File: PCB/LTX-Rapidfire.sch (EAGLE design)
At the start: 52 parts, among them J1 F-1X08-SIP-100-40Y, Q1 2N3904, Q10 SS8550D, Q11 2N3906, Q12 2N3906, Q13 2N3904, Q2 2N3906, Q3 2N3904, Q4 2N3904, Q5 2N3904, Q6 2N3906, Q7 2N3906, Q8 2N3906, Q9 2N3904, SW1 F-1X02-SIP-100-40, U2 Z8F082ADIL-8

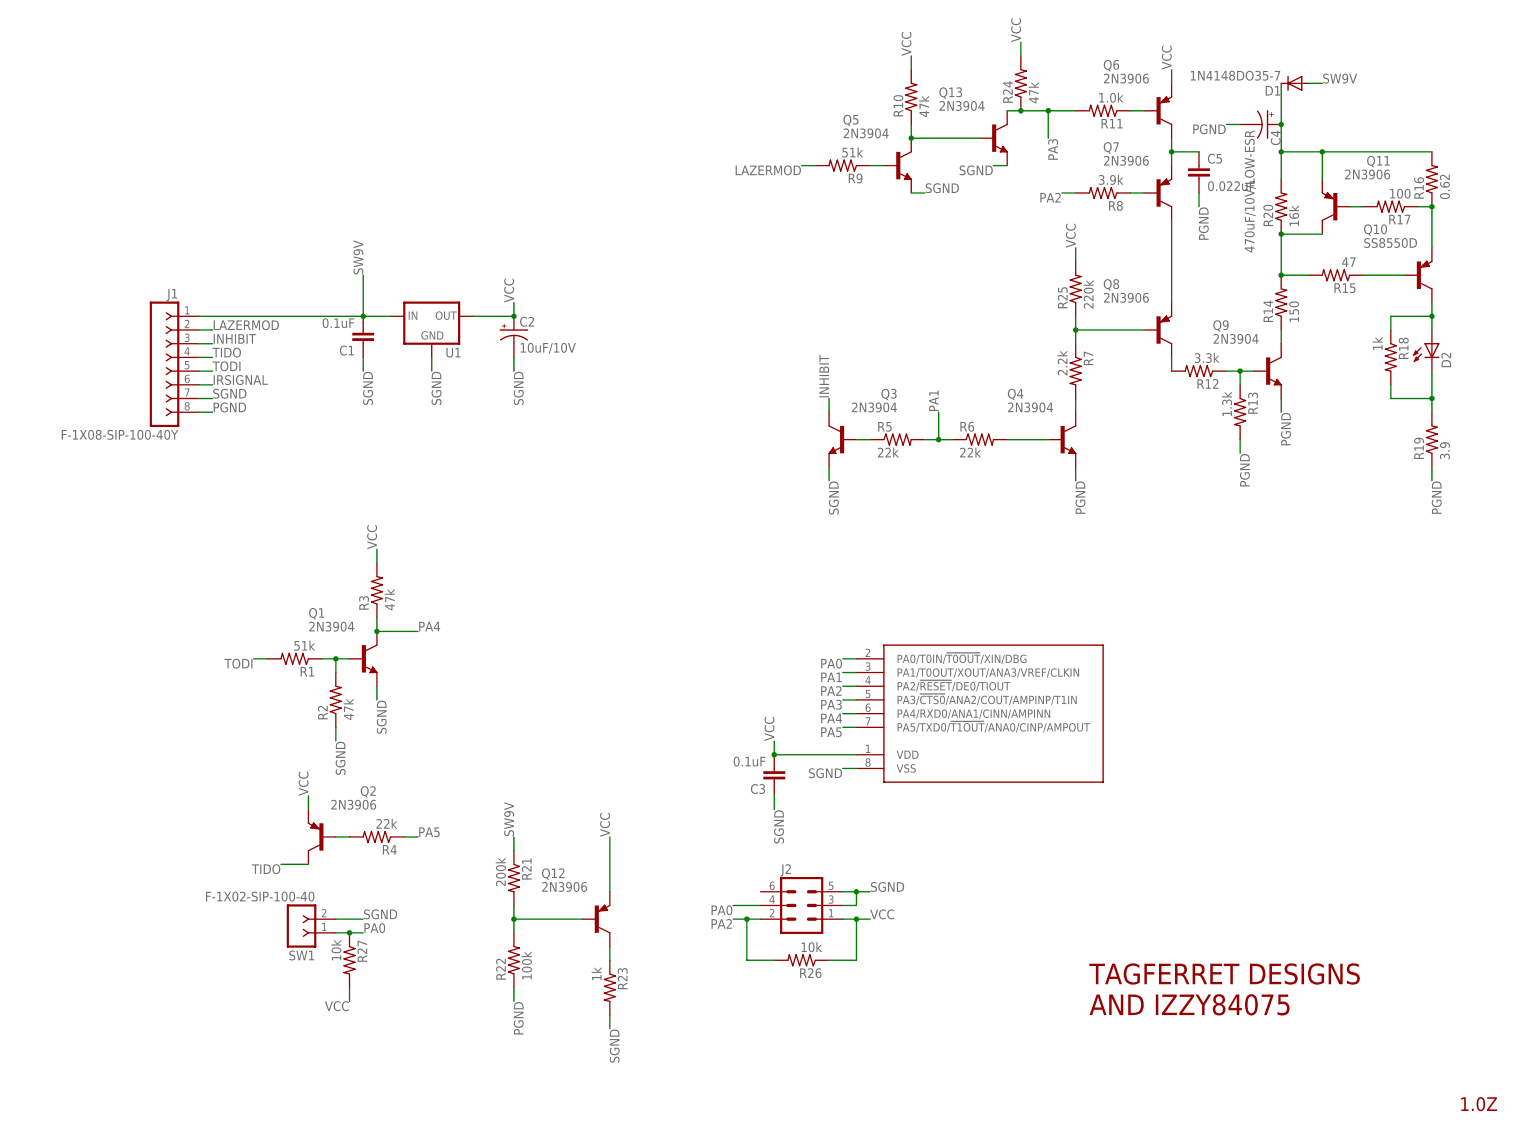
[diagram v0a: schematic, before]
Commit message: Labeled part numbers in schematic. Prep for SMD-ification
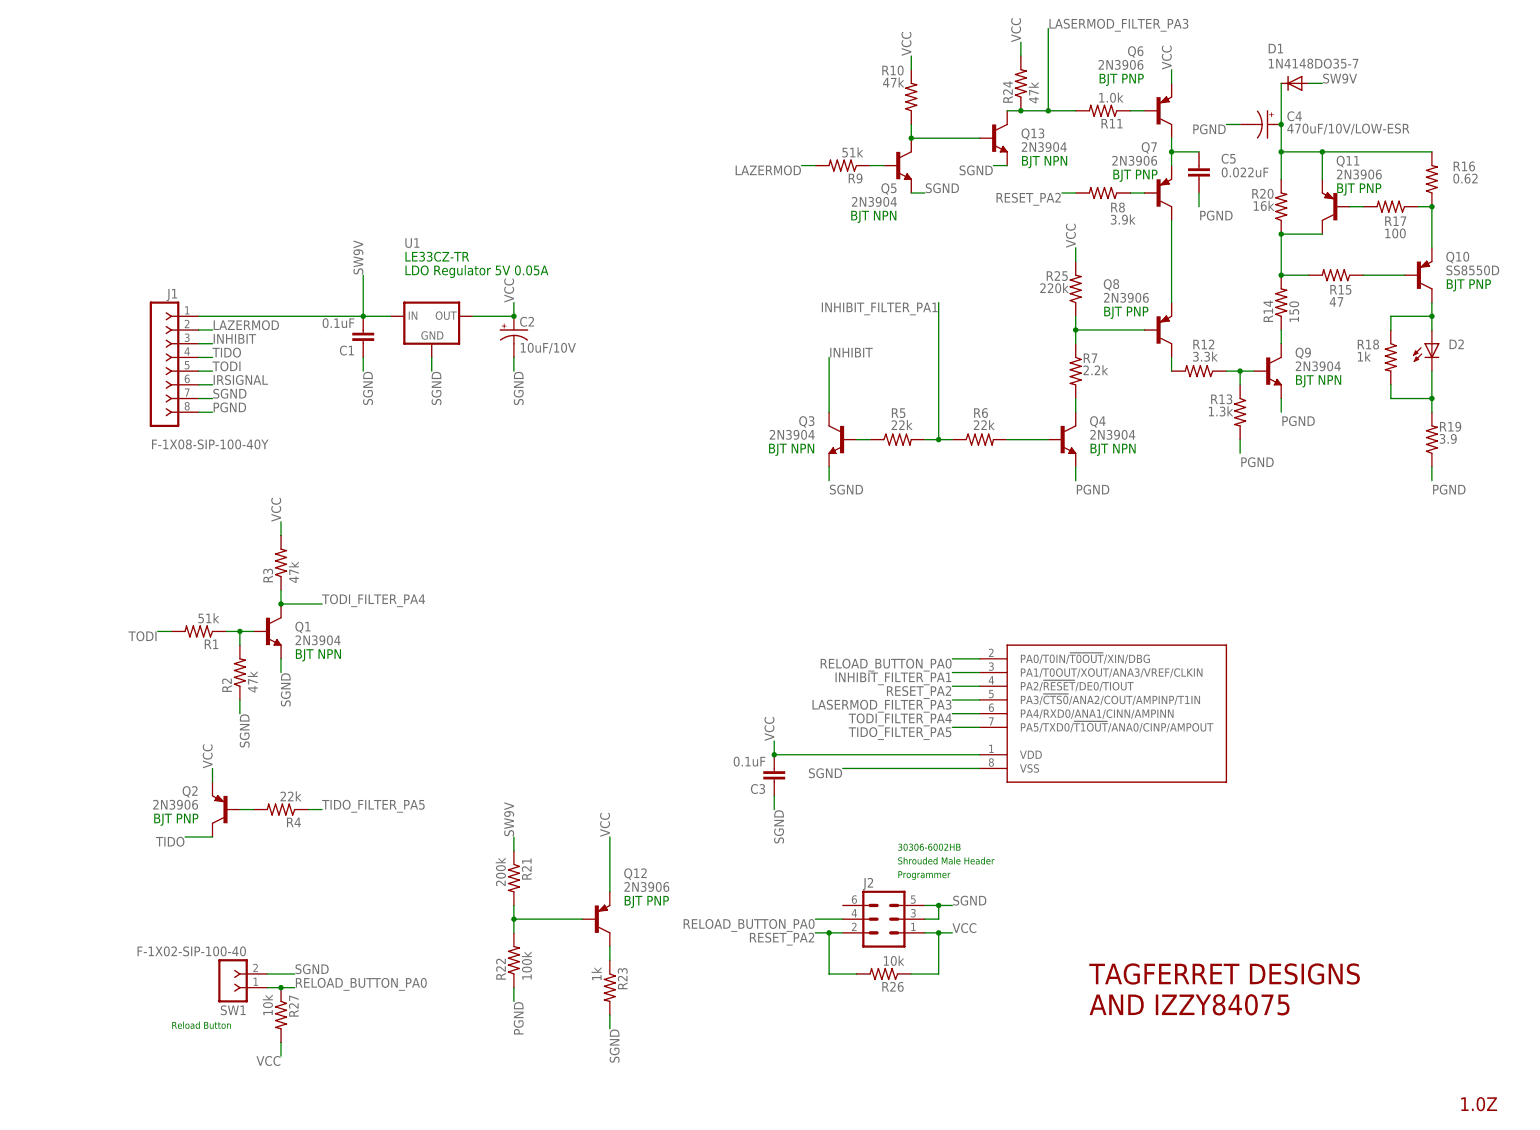
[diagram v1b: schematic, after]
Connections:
- net PA0 renamed RELOAD_BUTTON_PA0
- net PA1 renamed INHIBIT_FILTER_PA1
- net PA2 renamed RESET_PA2
- net PA3 renamed LASERMOD_FILTER_PA3
- net PA4 renamed TODI_FILTER_PA4
- net PA5 renamed TIDO_FILTER_PA5
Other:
- note added: "30306-6002HB"
- note added: "BJT NPN"
- note added: "BJT PNP"
- note added: "LDO Regulator 5V 0.05A"
- note added: "LE33CZ-TR"
- note added: "Programmer"
- note added: "Reload Button"
- note added: "Shrouded Male Header"
- moved on the sheet: J2, Q1, Q2, R1, R2, R26, R27, R3, R4, SW1

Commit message: Swapped basics to SMD
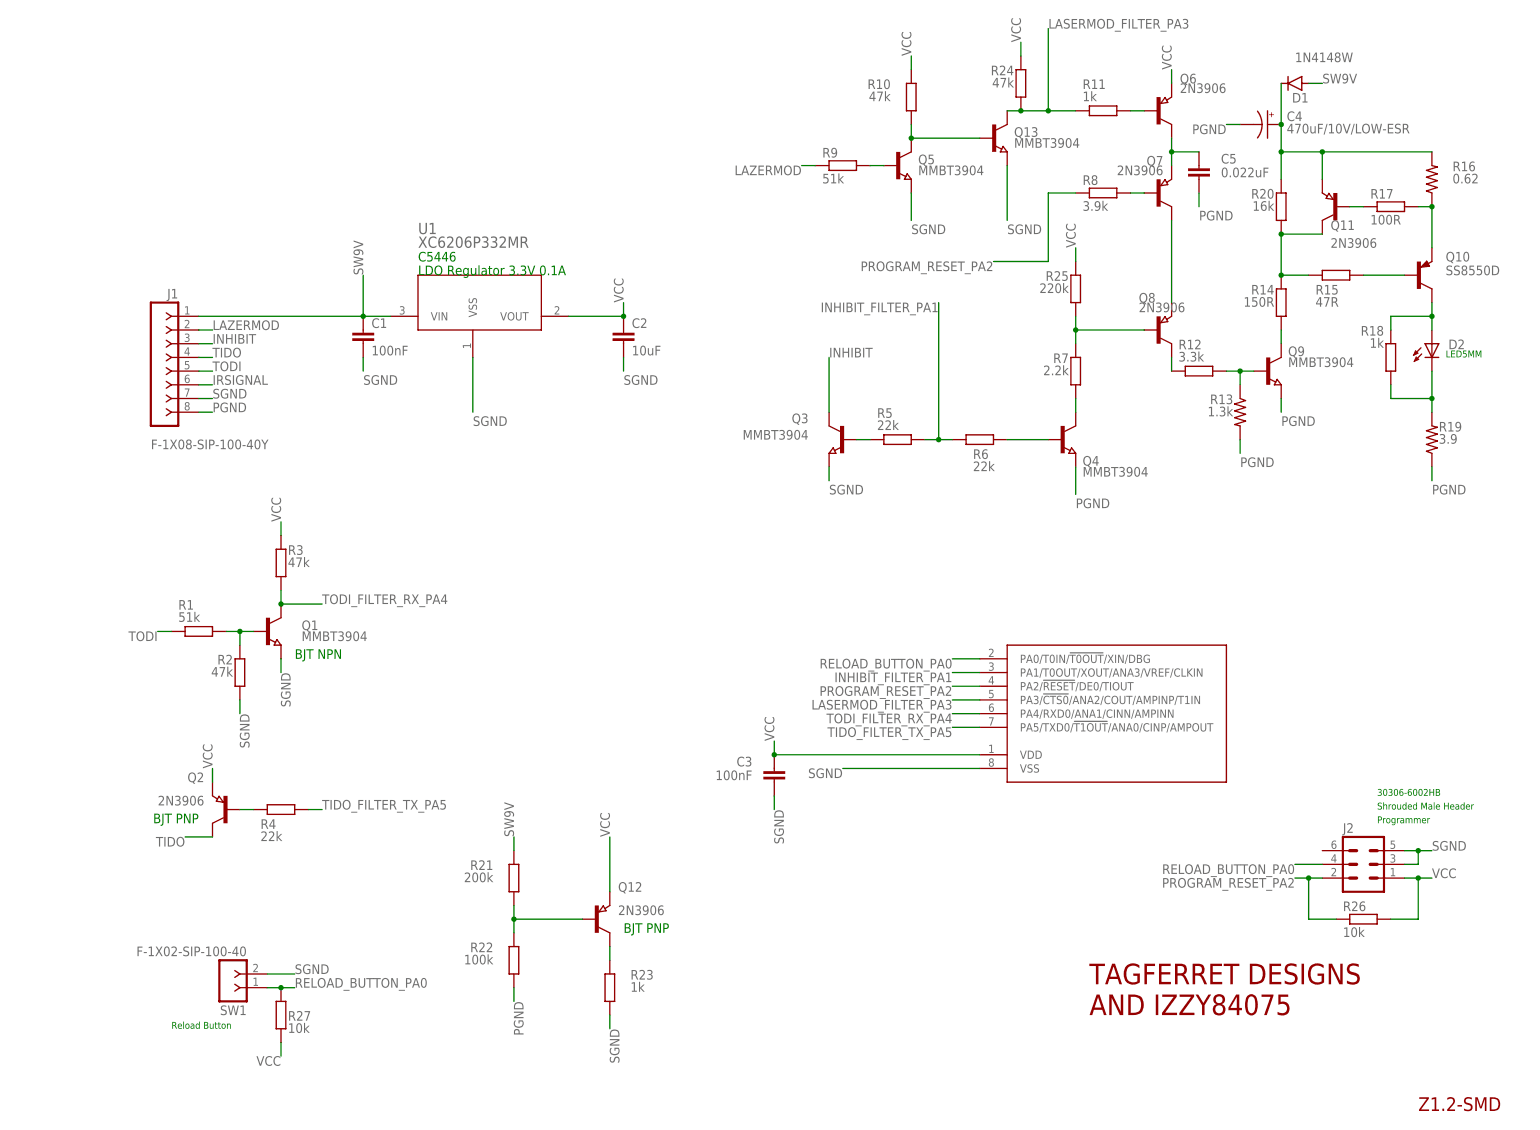
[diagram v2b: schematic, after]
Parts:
- C1, C3: value 0.1uF -> 100nF; device rcl:C-EU025-025X050 -> JLC PCB Basic Parts_loc:C_100NF/50V_0603
- C2: value 10uF/10V -> 10uF; device rcl:CPOL-USE2-4 -> JLC PCB Basic Parts_loc:C_10UF/25V_0603
- D1: value 1N4148DO35-7 -> 1N4148W; device diode:1N4148DO35-7 -> JLC PCB Basic Parts_loc:D_1N4148W_ST_SOD123
- Q1, Q13, Q3, Q4, Q5, Q9: value 2N3904 -> MMBT3904; device transistor:2N3904 -> JLC PCB Basic Parts_loc:T_NPN_MMBT3904_CHANGJ_SOT23-BEC
- Q11, Q12, Q2, Q6, Q7, Q8: device transistor-pnp:2N3906 -> JLC PCB Basic Parts_loc:T_PNP_MMBT5401_CHANGJ_SOT23-BEC; LCSC_DATASHEET (none) -> https://datasheet.lcsc.com/lcsc/1810111520_KEC-Semicon-2N39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; LCSC_PART (none) -> C147294; PROPERTIES (none) -> 40V 350mW 200mA 100@10mA,1V 250MHz 400mV@50mA,5mA PNP
- R1, R9: device rcl:R-US_0204/7 -> JLC PCB Basic Parts_loc:R_51K_0603
- R10, R2, R24, R3: device rcl:R-US_0204/2V -> JLC PCB Basic Parts_loc:R_47K_0603
- R11: value 1.0k -> 1k; device rcl:R-US_0204/7 -> JLC PCB Basic Parts_loc:R_1K_0603
- R12: device rcl:R-US_0204/7 -> JLC PCB Basic Parts_loc:R_3.3K_0603
- R14: value 150 -> 150R; device rcl:R-US_0204/7 -> JLC PCB Basic Parts_loc:R_150R_0603
- R15: value 47 -> 47R; device rcl:R-US_0204/7 -> JLC PCB Basic Parts_loc:R_47R_0603
- R17: value 100 -> 100R; device rcl:R-US_0204/2V -> JLC PCB Basic Parts_loc:R_100R_0603
- R18: device rcl:R-US_0204/2V -> JLC PCB Basic Parts_loc:R_1K_0603
- R20: device rcl:R-US_0204/2V -> JLC PCB Basic Parts_loc:R_16K_0805
- R21: device rcl:R-US_0204/7 -> JLC PCB Basic Parts_loc:R_200K_0603
- R22: device rcl:R-US_0204/2V -> JLC PCB Basic Parts_loc:R_100K_0603
- R23: device rcl:R-US_0204/7 -> JLC PCB Basic Parts_loc:R_1K_0603
- R25: device rcl:R-US_0204/2V -> JLC PCB Basic Parts_loc:R_220K_0603
- R26, R27: device rcl:R-US_0204/2V -> JLC PCB Basic Parts_loc:R_10K_0603
- R4, R5, R6: device rcl:R-US_0204/7 -> JLC PCB Basic Parts_loc:R_22K_0603
- R7: device rcl:R-US_0204/7 -> JLC PCB Basic Parts_loc:R_2.2K_0603
- R8: device rcl:R-US_0204/7 -> JLC PCB Basic Parts_loc:R_3.9K_0603
- U1: value (none) -> XC6206P332MR; device v-reg:78LXX -> LTX-Rapidfire:XC6206P332MR
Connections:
- net TODI_FILTER_PA4 renamed TODI_FILTER_RX_PA4
- removed net RESET_PA2: J2.2, R26.2, R8.2, U2.PA2/!RESET!/DE0/TIOUT
- removed net TIDO_FILTER_PA5: R4.1, U2.PA5/TXD0/!T1OUT!/ANA0/CINP/AMPOUT
- new net PROGRAM_RESET_PA2: J2.2, R26.1, R8.1, U2.PA2/!RESET!/DE0/TIOUT
- new net TIDO_FILTER_TX_PA5: R4.2, U2.PA5/TXD0/!T1OUT!/ANA0/CINP/AMPOUT
- net LASERMOD_FILTER_PA3: now also R11.1; no longer R11.2
- net LAZERMOD: now also R9.1; no longer R9.2
- net N$1: now also R17.1; no longer R17.2
- net N$10: now also R12.1; no longer R12.2
- net N$12: now also R7.2; no longer R7.1
- net N$13: now also R8.2; no longer R8.1
- net N$14: now also R7.1; no longer R7.2
- net N$17: now also R23.2; no longer R23.1
- net N$19: now also R11.2; no longer R11.1
- net N$20: now also R21.1; no longer R21.2
- net N$22: now also R9.2; no longer R9.1
- net N$24: now also R1.2; no longer R1.1
- net N$25: now also R4.1; no longer R4.2
- net N$3: now also R17.2; no longer R17.1
- net N$4: now also R15.1; no longer R15.2
- net N$5: now also R15.2; no longer R15.1
- net N$7: now also R18.1; no longer R18.2
- net N$8: now also R18.2; no longer R18.1
- net N$9: now also R12.2; no longer R12.1
- net RELOAD_BUTTON_PA0: now also R27.2; no longer R27.1
- net SGND: now also C1.2, C2.2, C3.2, R23.1, U1.VSS; no longer C1.1, C2.-, C3.1, R23.2, U1.GND
- net SW9V: now also C1.1, R21.2, U1.VIN; no longer C1.2, R21.1, U1.IN
- net TODI: now also R1.1; no longer R1.2
- net VCC: now also C2.1, C3.1, R26.2, R27.1, U1.VOUT; no longer C2.+, C3.2, R26.1, R27.2, U1.OUT
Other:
- note added: "C5446"
- note added: "LDO Regulator 3.3V 0.1A"
- note added: "LED5MM"
- note added: "Z1.2-SMD"
- note removed: "1.0Z"
- note removed: "LDO Regulator 5V 0.05A"
- note removed: "LE33CZ-TR"
- moved on the sheet: J2

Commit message: Part lists and gerbers for JLC
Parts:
- C4: LCSC (none) -> C43332; LCSC_PART (none) -> C43332
- C5: value 0.022uF -> 22nF; device rcl:C-EU025-025X050 -> JLC PCB Basic Parts_loc:C_22NF/50V_0603
- Q10: LCSC_PART (none) -> C118551
- R13: device rcl:R-US_0204/2V -> JLC PCB Basic Parts_loc:R_2.2K_0603; LCSC_DATASHEET (none) -> https://datasheet.lcsc.com/lcsc/2206010130_UNI-ROYAL-Uniroy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; LCSC_PART (none) -> C22767; PROPERTIES (none) -> 100mW Thick Film Resistors 75V ±100ppm/℃ ±1% -55℃~+155℃ 1.3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
- R16: value 0.62 -> 0.62R 1W; device rcl:R-US_0204/7 -> resistor:R-US_R2512; LCSC_PART (none) -> C705623
- R19: value 3.9 -> 3.9R 1W; device rcl:R-US_0207/10 -> resistor:R-US_R2512; LCSC_PART (none) -> C66801
- U1: LCSC_PART (none) -> C5446
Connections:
- net N$9: now also R13.2; no longer R13.1
- net PGND: now also R13.1; no longer R13.2
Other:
- note added: "1W 1.5A"

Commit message: Swapped chip and routed pcb
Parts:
- removed C3: 100nF, JLC PCB Basic Parts_loc:C_100NF/50V_0603
- removed J2: (no value), izzy:MA03-2
- removed R26: 10k, JLC PCB Basic Parts_loc:R_10K_0603
- removed U2: Z8F082ADIL-8, izzy:Z8F082ADIL-8
- added C6: 100nF, JLC PCB Basic Parts_loc:C_100NF/50V_0603
- added JP1: (no value), adafruit:PINHD-1X3
- added R28: 1K, SparkFun-Resistors:2.2KOHM-0402-1/16W-1%
- added U3: ATTINY1616-MNRVQFN20_3X3_MCH-M, attiny1616:ATTINY1616-MNRVQFN20_3X3_MCH-M
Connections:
- net INHIBIT renamed INHIBIT_OUT
- net LAZERMOD renamed LAZERMOD_IN
- net N$2 renamed PROTECTED_9V
- net SW9V renamed +9V
- removed net INHIBIT_FILTER_PA1: R5.2, R6.1, U2.PA1/T0OUT/XOUT/ANA3/VREF/CLKIN
- removed net LASERMOD_FILTER_PA3: Q13.C, R11.1, R24.1, U2.PA3/!CTS0!/ANA2/COUT/AMPINP/T1IN
- removed net PROGRAM_RESET_PA2: J2.2, R26.1, R8.1, U2.PA2/!RESET!/DE0/TIOUT
- removed net RELOAD_BUTTON_PA0: J2.4, R27.2, SW1.1, U2.PA0/T0IN/!T0OUT!/XIN/DBG
- removed net TIDO_FILTER_TX_PA5: R4.2, U2.PA5/TXD0/!T1OUT!/ANA0/CINP/AMPOUT
- removed net TODI_FILTER_RX_PA4: Q1.C, R3.1, U2.PA4/RXD0/ANA1/CINN/AMPINN
- new net INHIBIT_PB1: R5.2, R6.1, U3.PB1
- new net LASERMOD_IN_PB3: Q13.C, R11.1, R24.1, U3.TOSC/PB3
- new net PROGRAM_RESET_PA0: R28.1, R8.1, U3.PA0/!RESET/UPDI
- new net RELOAD_BUTTON_PB0: R27.2, SW1.2, U3.PB0
- new net TIDO_FILTER_TX_PA1: R4.2, U3.PA1
- new net TODI_FILTER_RX_PA2: Q1.C, R3.1, U3.PA2
- new net UPDI: JP1.3, R28.2
- net SGND: now also C6.2, JP1.2, SW1.1, U3.GND; no longer C3.2, J2.3, J2.5, SW1.2, U2.VSS
- net VCC: now also C6.1, JP1.1, U3.VDD; no longer C3.1, J2.1, R26.2, U2.VDD
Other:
- note added: "0 16 15"
- note added: "10 9 8 7 6"
- note added: "14 13 12 11"
- note added: "5 4 3 2 1"
- note added: "ARDUINO"
- note added: "C507118"
- note added: "Dustin Westaby"
- note added: "GND"
- note added: "PWR"
- note added: "UART RX"
- note added: "UART TX"
- note added: "UPDI"
- note added: "UPDI Programming Header"
- note added: "WestabyElectronics.com"
- note removed: "30306-6002HB"
- note removed: "Programmer"
- note removed: "Shrouded Male Header"

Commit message: Updated gerbers, com, and placement
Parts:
- removed R28: 1K, SparkFun-Resistors:2.2KOHM-0402-1/16W-1%
- added R26: 1k, JLC PCB Basic Parts_loc:R_1K_0603
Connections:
- net PROGRAM_RESET_PA0: now also R26.1; no longer R28.1
- net UPDI: now also R26.2; no longer R28.2
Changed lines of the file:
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@@
 <attribute name="LCSC_PART" value="C66801"/>
 </part>
-<part name="R28" library="SparkFun-Resistors" deviceset="2.2KOHM" device="-0402-1/16W-1%" value="1K"/>
 <part name="SUPPLY10" library="supply2" deviceset="GND" device=""/>
 <part name="SUPPLY2" library="supply2" deviceset="GND" device=""/>
@@
 <part name="SUPPLY16" library="supply2" deviceset="+9V" device=""/>
 <part name="JP1" library="adafruit" deviceset="PINHD-1X3" device=""/>
+<part name="R26" library="JLC PCB Basic Parts_loc" deviceset="R_" device="_0603" technology="1K" value="1k"/>
 </parts>
 <sheets>
@@
 </plain>
 <instances>
-<instance part="R28" gate="G$1" x="35.56" y="93.98" rot="MR0"/>
 <instance part="SUPPLY10" gate="GND" x="22.86" y="53.34" rot="MR0"/>
 <instance part="SUPPLY2" gate="GND" x="38.1" y="35.56" rot="MR0"/>
@@
 <instance part="SUPPLY16" gate="G$1" x="58.42" y="157.48"/>
 <instance part="JP1" gate="A" x="226.06" y="144.78"/>
+<instance part="R26" gate="R1" x="35.56" y="93.98" smashed="yes" rot="R180">
+<attribute name="NAME" x="34.0614" y="97.79" size="1.778" layer="95" rot="R90"/>
+<attribute name="VALUE" x="36.322" y="97.79" size="1.778" layer="96" rot="R90"/>
+</instance>
 </instances>
 <busses>
@@
 <net name="UPDI" class="0">
 <segment>
-<pinref part="R28" gate="G$1" pin="2"/>
 <wire x1="30.48" y1="93.98" x2="20.32" y2="93.98" width="0.1524" layer="91"/>
 <label x="20.32" y="93.98" size="1.778" layer="95"/>
+<pinref part="R26" gate="R1" pin="2"/>
 </segment>
 <segment>
@@
 <net name="PROGRAM_RESET_PA0" class="0">
 <segment>
-<pinref part="R28" gate="G$1" pin="1"/>
 <wire x1="40.64" y1="93.98" x2="48.26" y2="93.98" width="0.1524" layer="91"/>
 <pinref part="U3" gate="A" pin="PA0/!RESET/UPDI"/>
@@
 <wire x1="48.26" y1="104.14" x2="50.8" y2="104.14" width="0.1524" layer="91"/>
 <label x="50.8" y="104.14" size="1.778" layer="95"/>
-</segment>
-</net>
+<pinref part="R26" gate="R1" pin="1"/>
+</segment>
+</net>
